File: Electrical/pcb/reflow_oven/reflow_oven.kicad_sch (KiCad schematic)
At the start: 0 parts

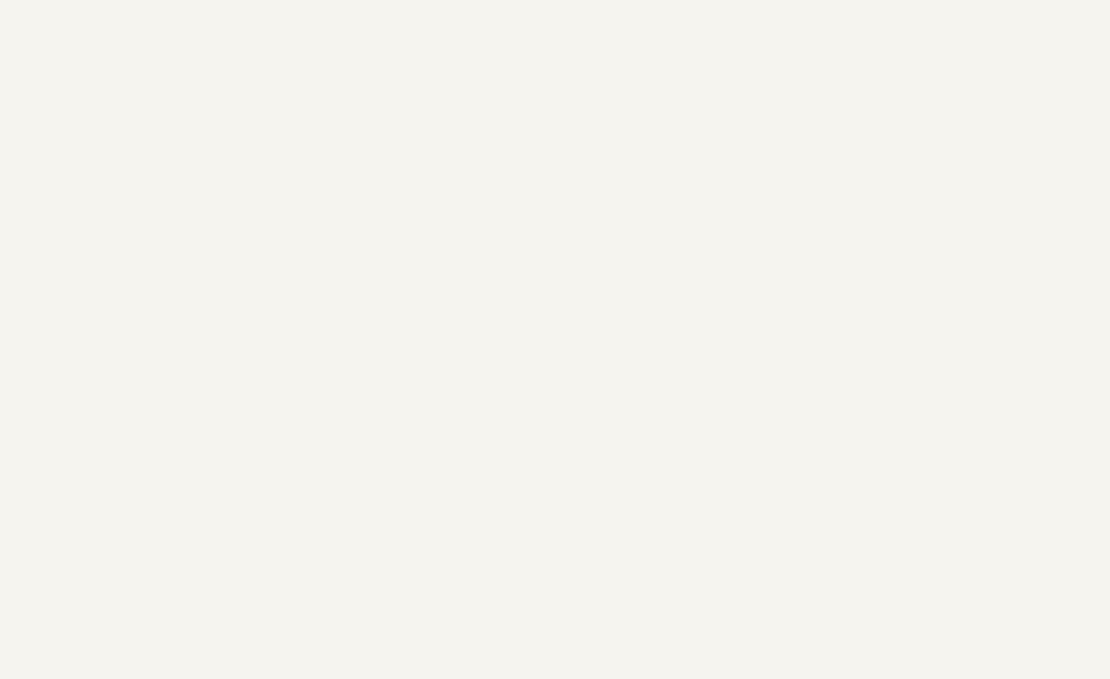
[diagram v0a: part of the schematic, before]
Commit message: schematic
added microcontrroller and .ioc file
added usb serial converter
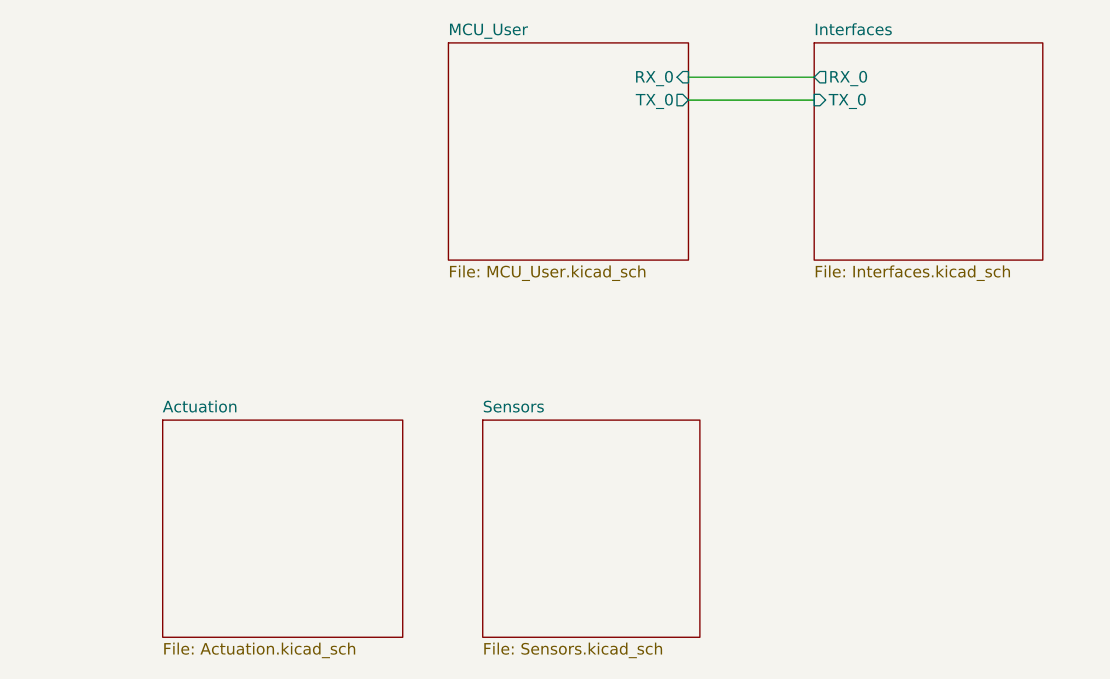
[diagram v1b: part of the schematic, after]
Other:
- added sheet Actuation (Actuation.kicad_sch)
- added sheet Interfaces (Interfaces.kicad_sch)
- added sheet MCU_User (MCU_User.kicad_sch)
- added sheet Sensors (Sensors.kicad_sch)

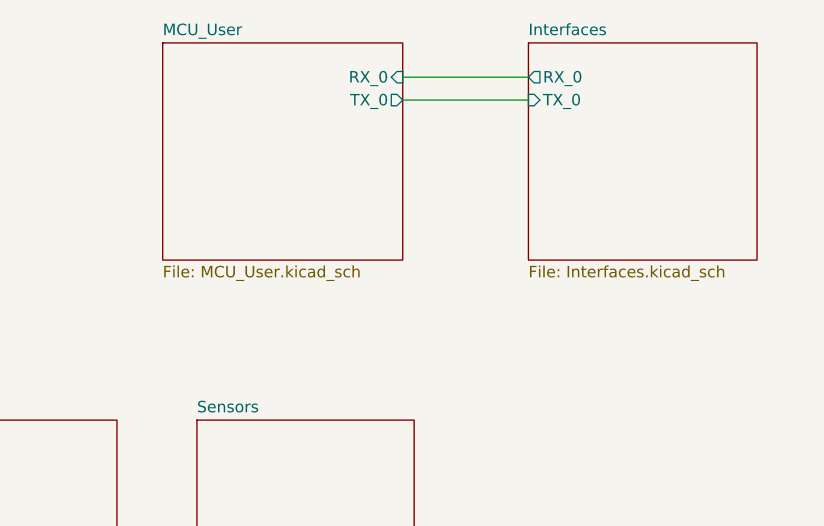
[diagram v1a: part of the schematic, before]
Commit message: interface
partial interface schematic
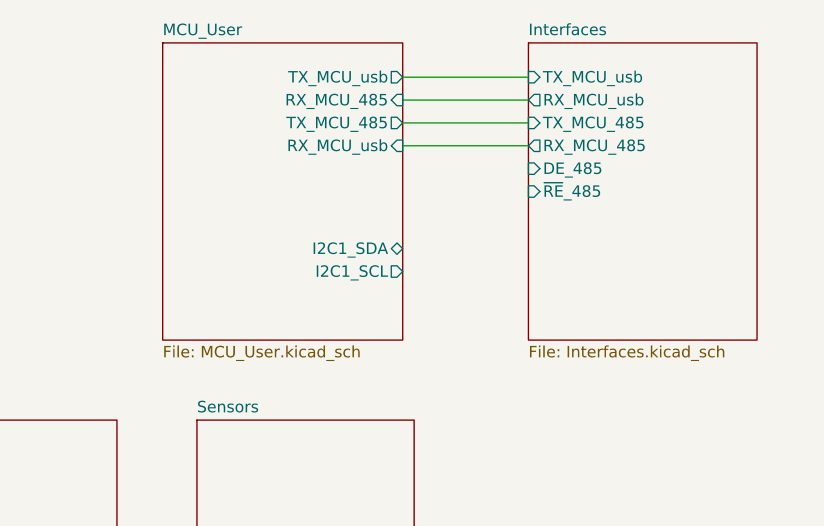
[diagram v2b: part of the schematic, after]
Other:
- sheet Interfaces ports: added DE_485, RX_MCU_485, RX_MCU_usb, TX_MCU_485, TX_MCU_usb, ~{RE}_485; removed RX_0, TX_0
- sheet MCU_User ports: added I2C1_SCL, I2C1_SDA, RX_MCU_485, RX_MCU_usb, TX_MCU_485, TX_MCU_usb; removed RX_0, TX_0

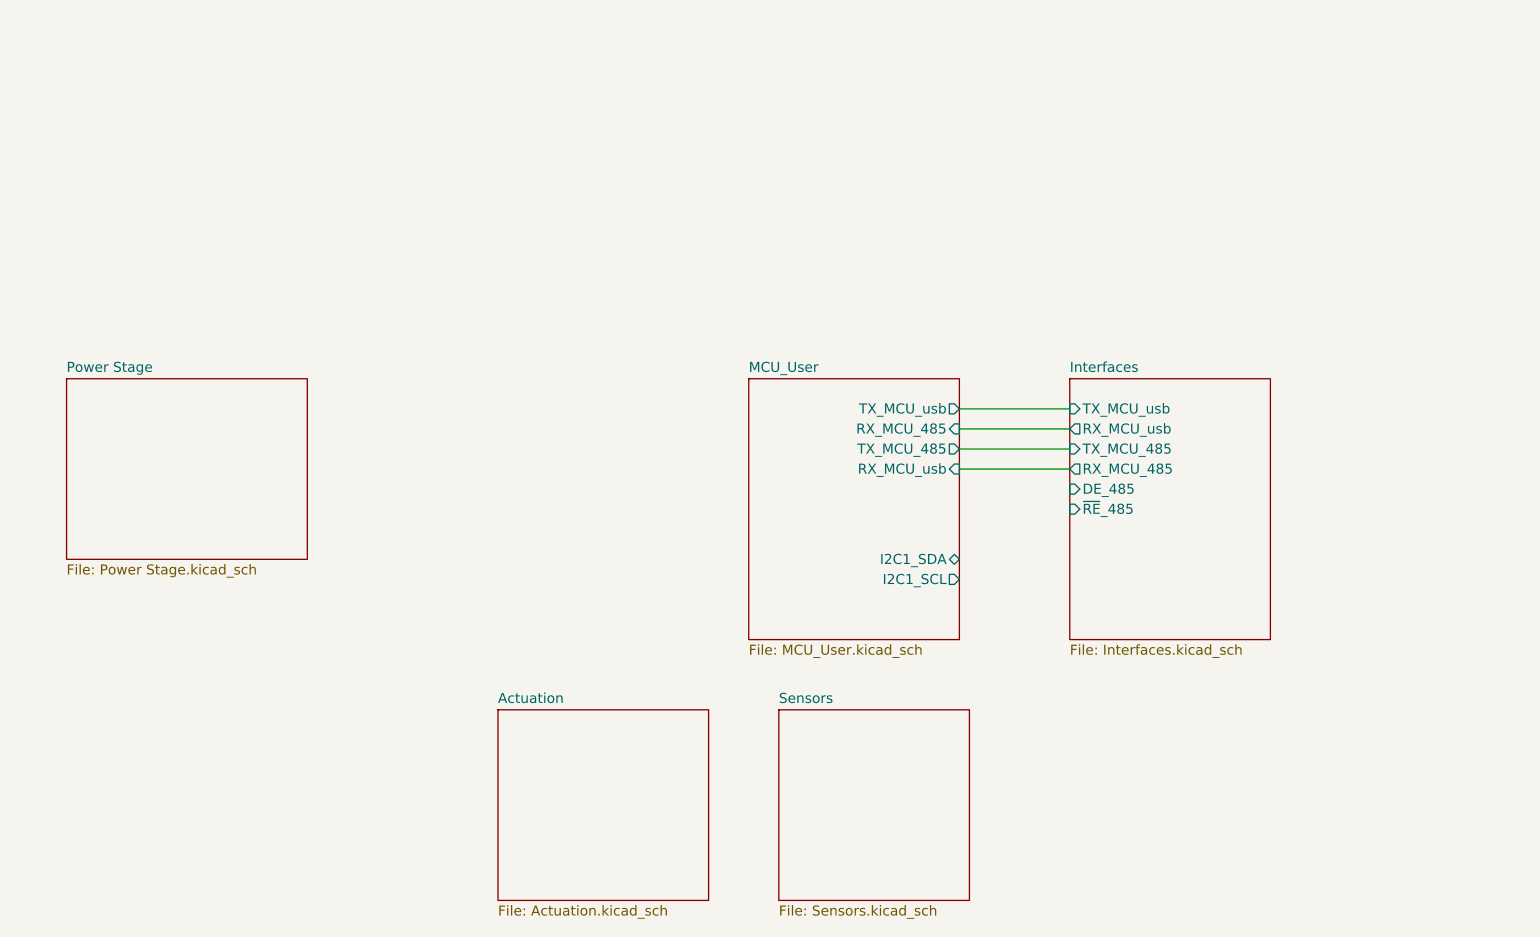
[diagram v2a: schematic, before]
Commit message: analog Sensing
-voltage and current sensor
-zero crossing
-temperature
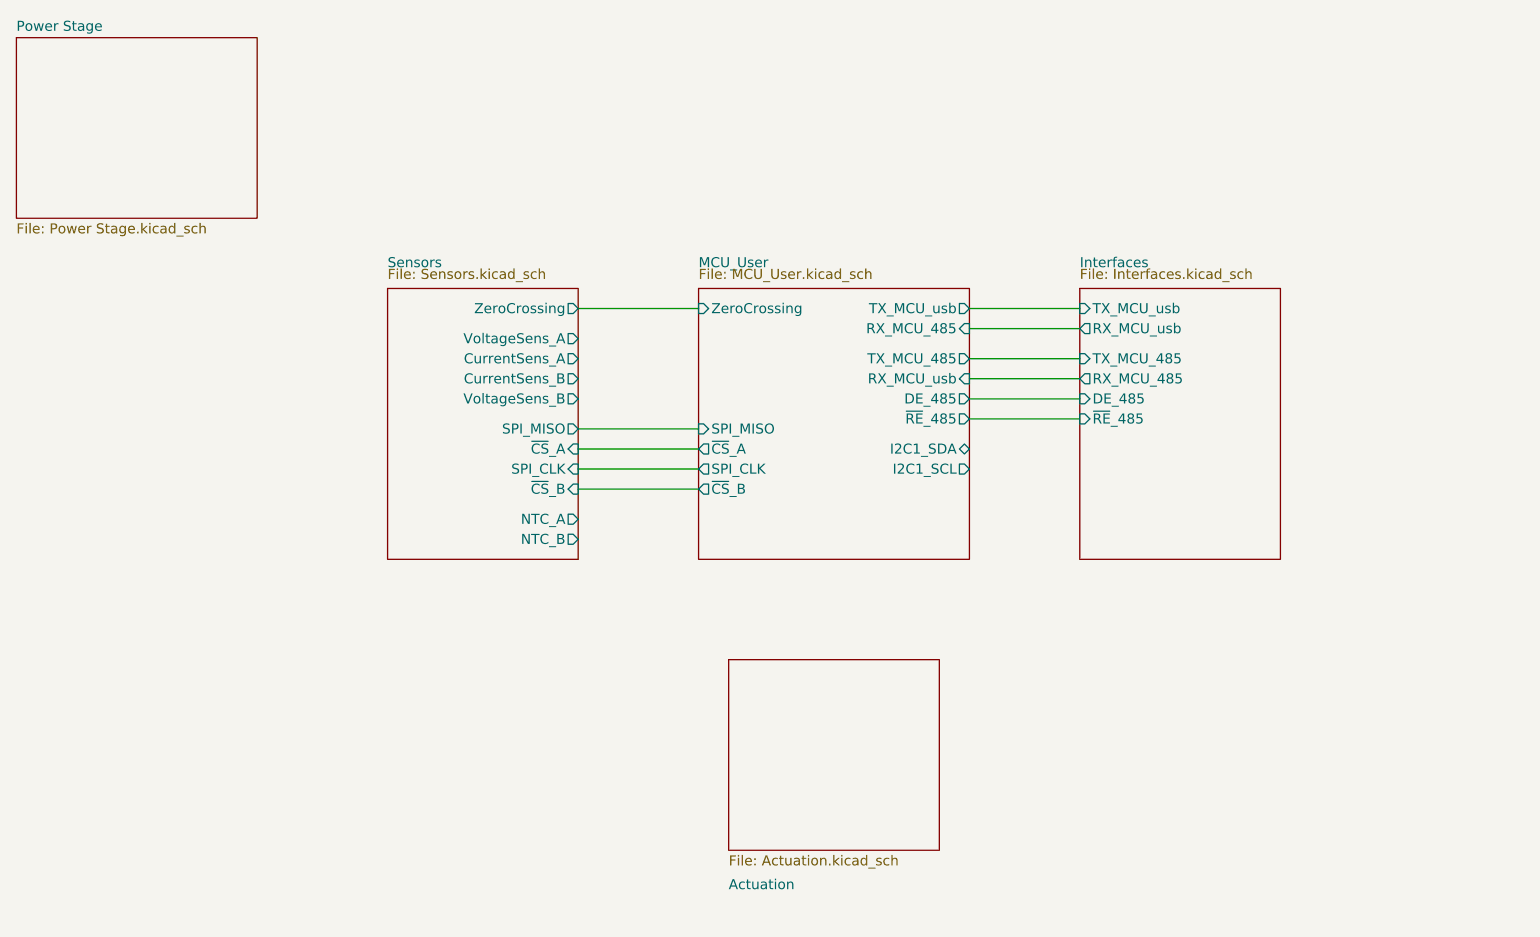
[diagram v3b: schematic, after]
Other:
- sheet MCU_User ports: added DE_485, SPI_CLK, SPI_MISO, ZeroCrossing, ~{CS}_A, ~{CS}_B, ~{RE}_485; removed none
- sheet Sensors ports: added CurrentSens_A, CurrentSens_B, NTC_A, NTC_B, SPI_CLK, SPI_MISO, VoltageSens_A, VoltageSens_B, ZeroCrossing, ~{CS}_A, ~{CS}_B; removed none

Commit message: schematic
-interface
-micro
todo
output
routing
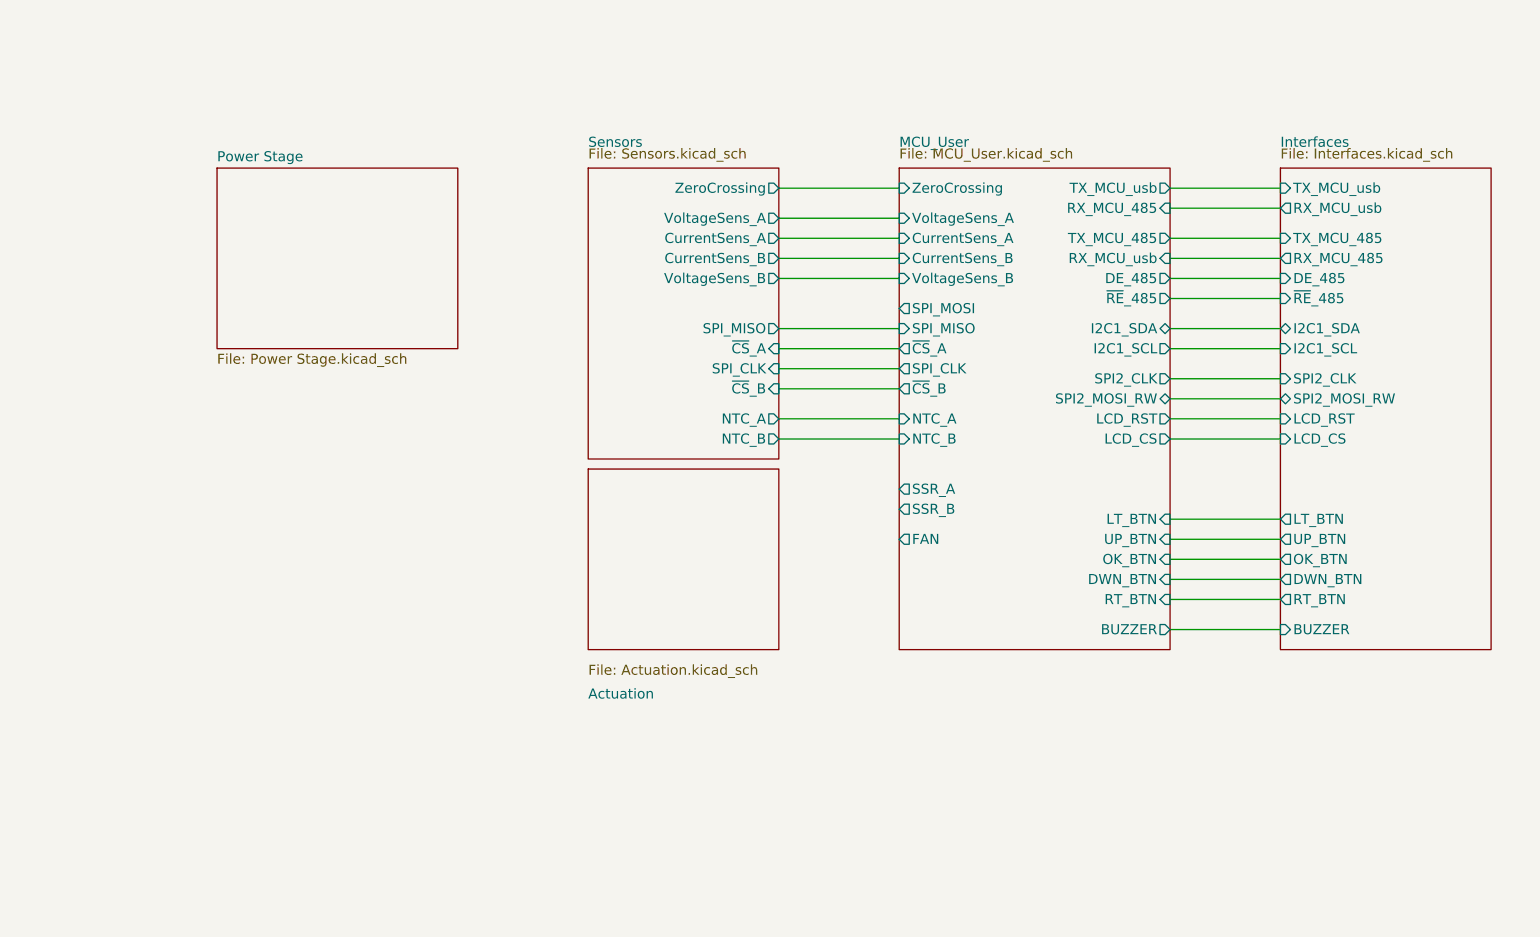
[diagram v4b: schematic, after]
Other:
- sheet Interfaces ports: added BUZZER, DWN_BTN, I2C1_SCL, I2C1_SDA, LCD_CS, LCD_RST, LT_BTN, OK_BTN, RT_BTN, SPI2_CLK, SPI2_MOSI_RW, UP_BTN; removed none
- sheet MCU_User ports: added BUZZER, CurrentSens_A, CurrentSens_B, DWN_BTN, FAN, LCD_CS, LCD_RST, LT_BTN, NTC_A, NTC_B, OK_BTN, RT_BTN, SPI2_CLK, SPI2_MOSI_RW, SPI_MOSI, SSR_A, SSR_B, UP_BTN, VoltageSens_A, VoltageSens_B; removed none
